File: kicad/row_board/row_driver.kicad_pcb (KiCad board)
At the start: 2 copper layers, 76 parts, among them J1 Panel row connector (female), J2 Row daisy chain connector (ma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, J5 EXT_CONTROL, J6 Barrel_Jack, Q1 2N3904, U1 TPIC6B595, U10 TXB0108-PWR, U2 TPIC6B595, U3 TBD62783, U4 TPIC6B595, U5 TPIC6B595, U6 TBD62783, U7 WE-FDSM_DC/DC_5V, U8 4N25, U9 WeMos_mini

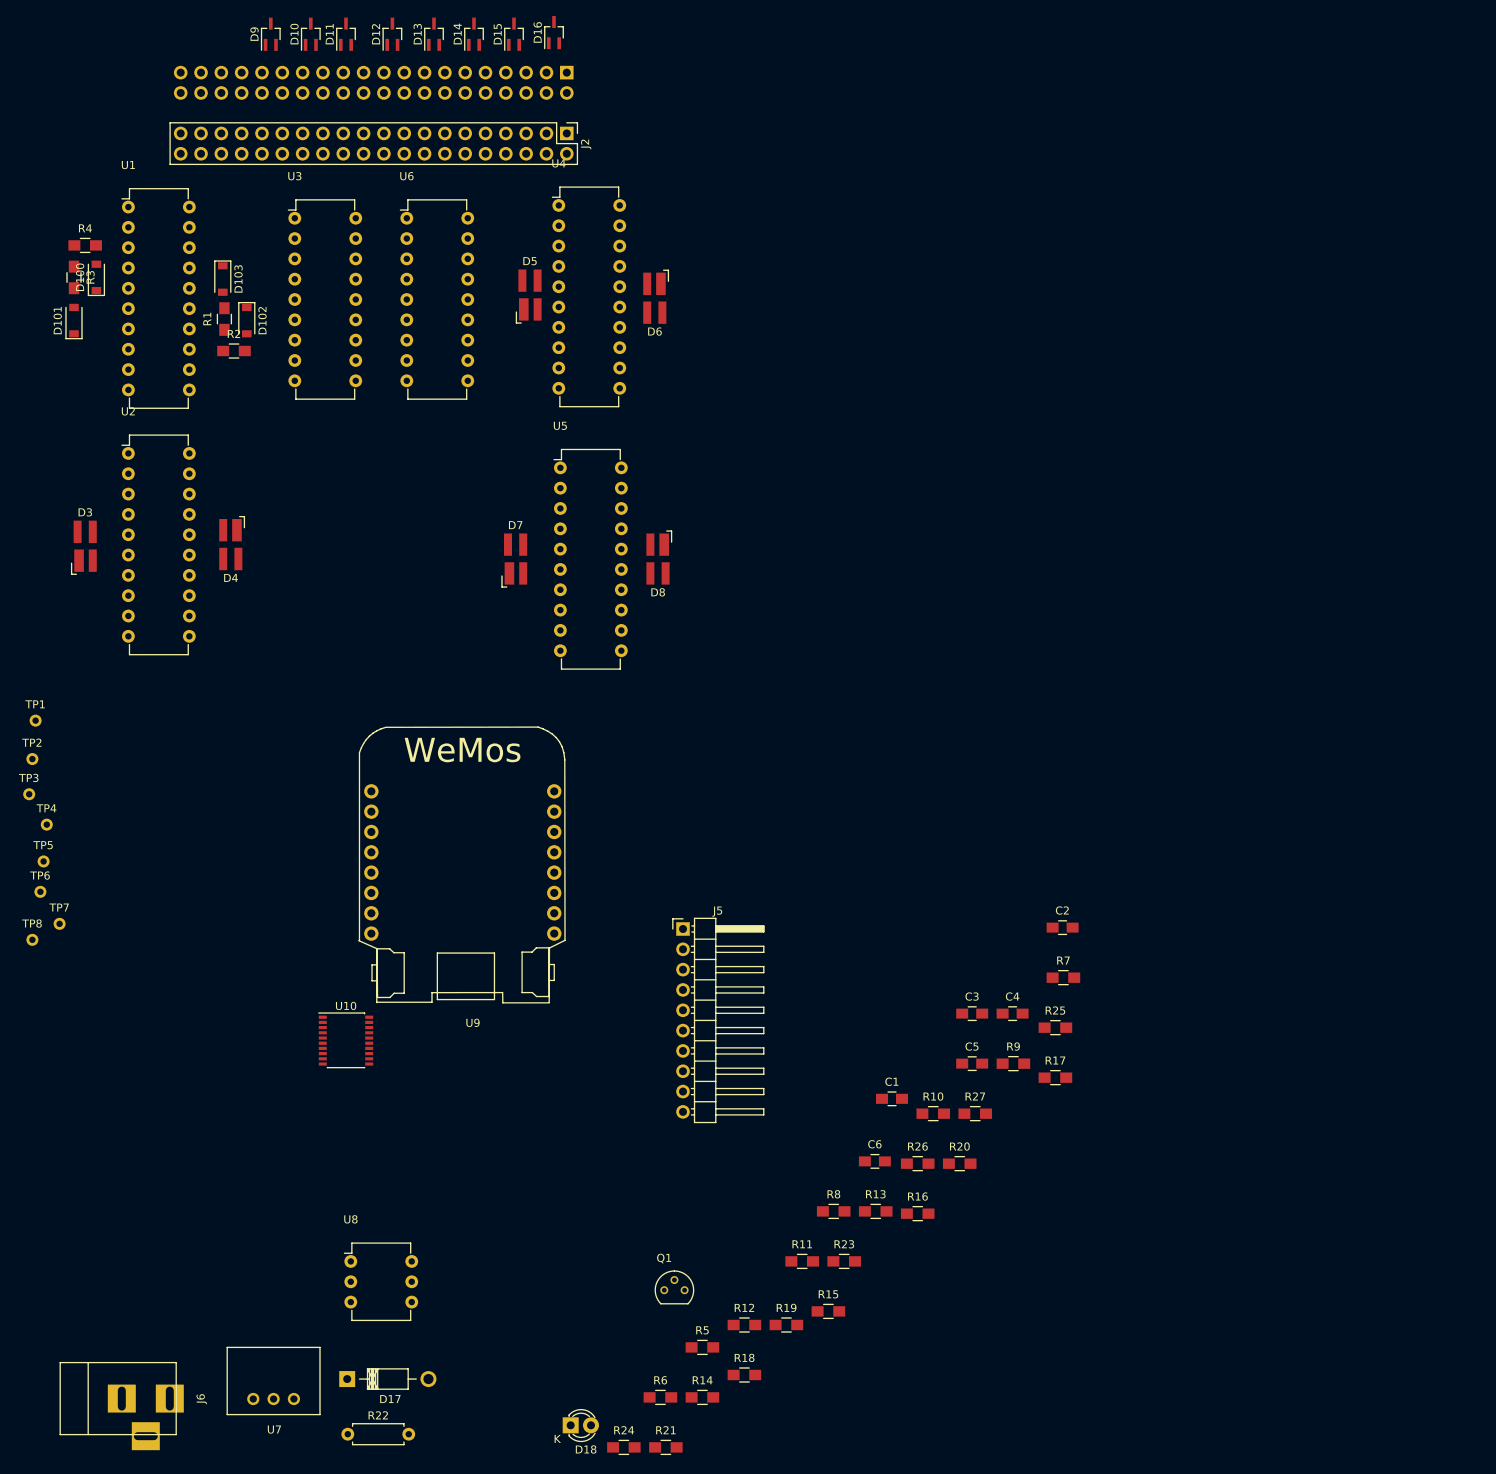
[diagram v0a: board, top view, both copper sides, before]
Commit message: Replace BAV23 with BAS16GW
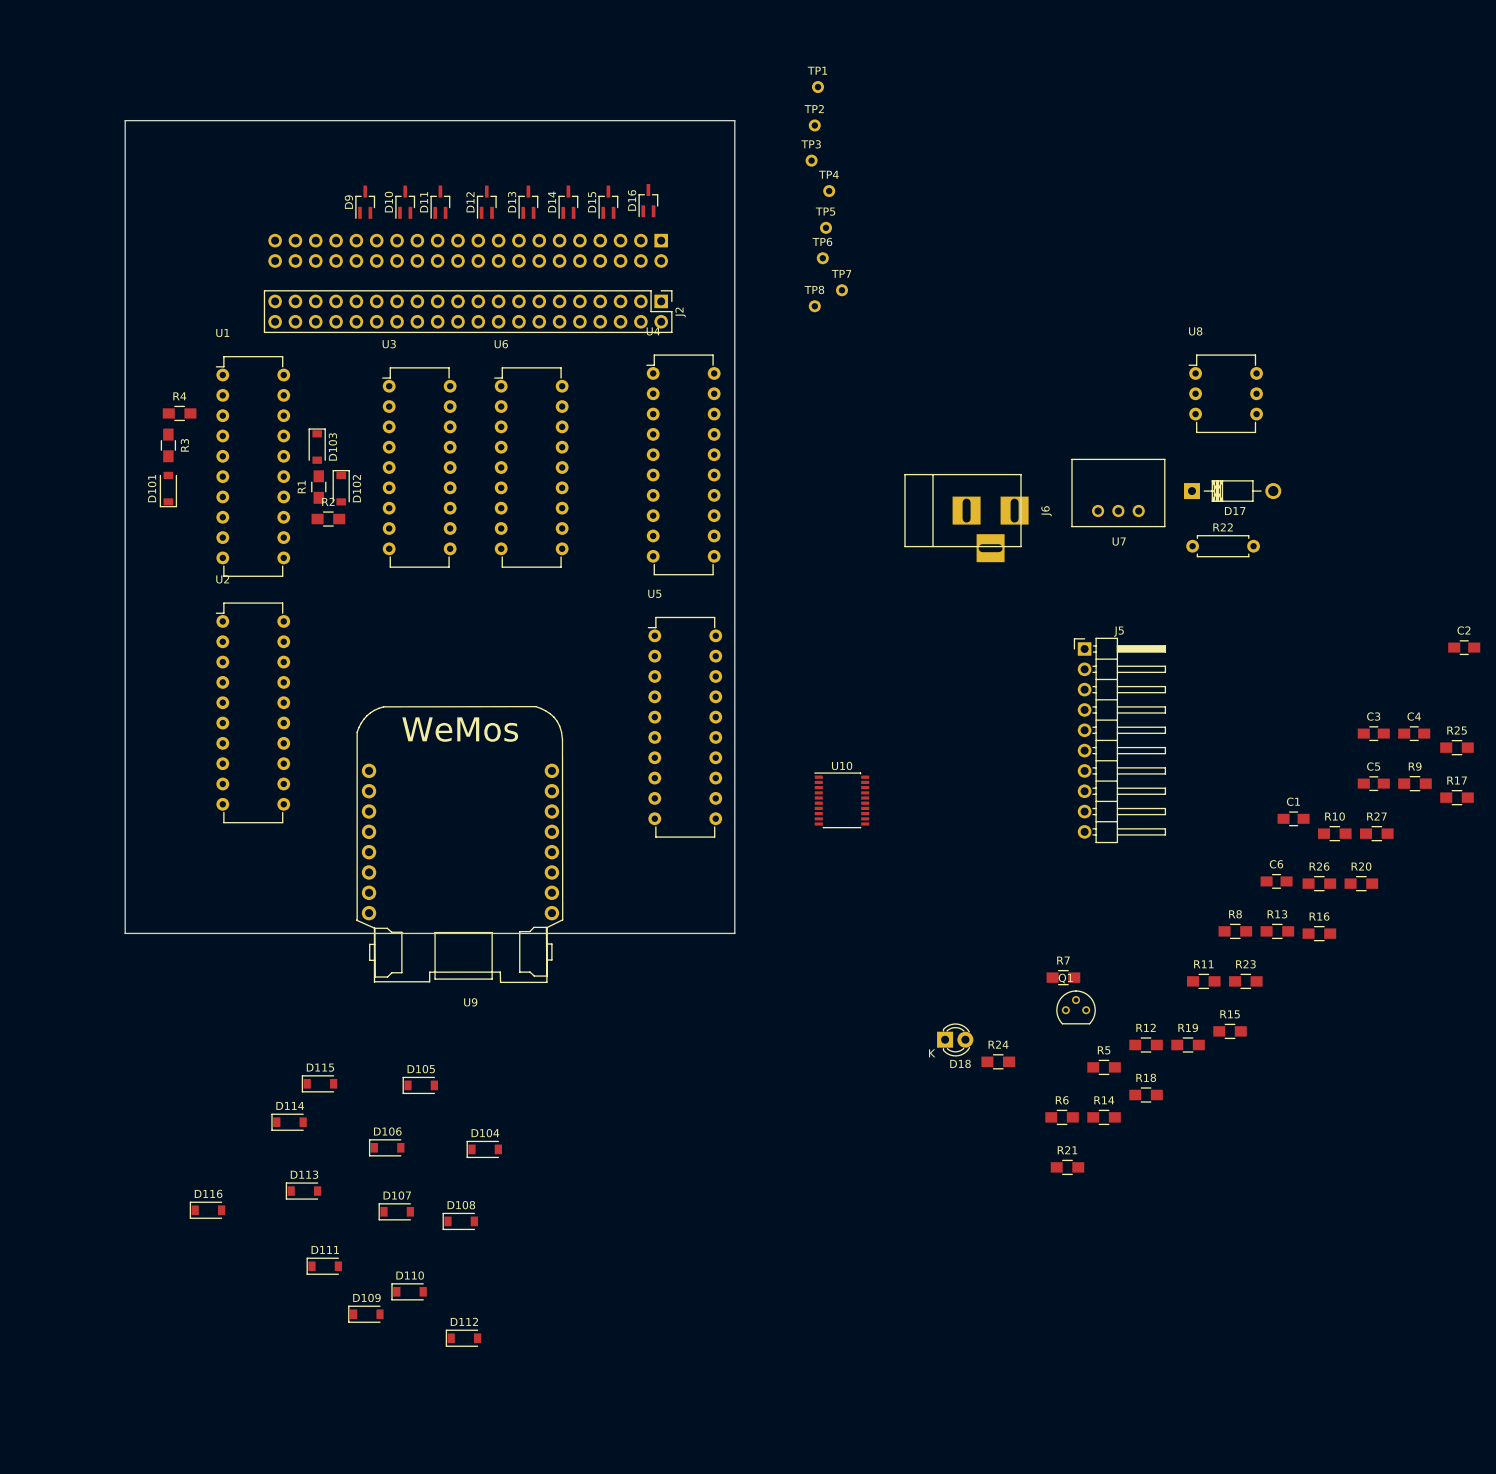
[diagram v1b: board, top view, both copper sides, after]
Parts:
- removed D100: D, Diodes_SMD:D_SOD-123
- removed D3, D4, D5, D6, D7, D8: BAV23, TO_SOT_Packages_SMD:SOT-143_Handsoldering
- added D104: BAS16GW, Diodes_SMD:D_SOD-123, F.Cu at (95.8, 154.0)
- added D105: BAS16GW, Diodes_SMD:D_SOD-123, F.Cu at (87.8, 146.0)
- added D106: BAS16GW, Diodes_SMD:D_SOD-123, F.Cu at (83.6, 153.8)
- added D107: BAS16GW, Diodes_SMD:D_SOD-123, F.Cu at (84.8, 161.8)
- added D108: BAS16GW, Diodes_SMD:D_SOD-123, F.Cu at (92.8, 163.0)
- added D109: BAS16GW, Diodes_SMD:D_SOD-123, F.Cu at (81.0, 174.6)
- added D110: BAS16GW, Diodes_SMD:D_SOD-123, F.Cu at (86.4, 171.8)
- added D111: BAS16GW, Diodes_SMD:D_SOD-123, F.Cu at (75.8, 168.6)
- added D112: BAS16GW, Diodes_SMD:D_SOD-123, F.Cu at (93.2, 177.6)
- added D113: BAS16GW, Diodes_SMD:D_SOD-123, F.Cu at (73.2, 159.2)
- added D114: BAS16GW, Diodes_SMD:D_SOD-123, F.Cu at (71.4, 150.6)
- added D115: BAS16GW, Diodes_SMD:D_SOD-123, F.Cu at (75.2, 145.8)
- added D116: BAS16GW, Diodes_SMD:D_SOD-123, F.Cu at (61.2, 161.6)
- D101, D102, D103: value D -> BAS16GW
- moved R22 153.2 mm to (184.2, 78.6)
- moved U8 153.2 mm to (184.6, 57.0)
- moved D17 153.2 mm to (184.1, 71.7)
- moved J6 153.2 mm to (155.8, 74.1)
- moved U7 153.2 mm to (174.9, 71.9)
- moved TP2 125.8 mm to (137.0, 26.0)
- moved TP1 125.8 mm to (137.4, 21.2)
- moved TP4 125.8 mm to (138.8, 34.2)
- moved TP5 125.8 mm to (138.4, 38.8)
- moved TP7 125.8 mm to (140.4, 46.6)
- moved TP3 125.8 mm to (136.6, 30.4)
- moved TP6 125.8 mm to (138.0, 42.6)
- moved TP8 125.8 mm to (137.0, 48.6)
- moved U10 68.9 mm to (140.4, 110.4)
- moved D18 67.2 mm to (153.3, 140.3)
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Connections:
- D101 pad 1: ROW15_L -> ROW16_L
- D102 pad 1: ROW14_L -> ROW15_L
- D103 pad 1: ROW13_L -> ROW14_L
- R1 pad 2: Net-(D103-Pad2) -> Net-(D104-Pad2)
- R2 pad 2: Net-(D102-Pad2) -> Net-(D103-Pad2)
- R3 pad 2: Net-(D101-Pad2) -> Net-(D102-Pad2)
- R4 pad 2: Net-(D100-Pad2) -> Net-(D101-Pad2)
- U1 pad 14: Net-(D102-Pad2) -> Net-(D103-Pad2)
- U1 pad 16: Net-(D103-Pad2) -> Net-(D104-Pad2)
- U1 pad 4: Net-(D100-Pad2) -> Net-(D101-Pad2)
- U1 pad 6: Net-(D101-Pad2) -> Net-(D102-Pad2)
- U3 pad 1: Net-(D100-Pad2) -> Net-(D101-Pad2)
- U3 pad 2: Net-(D101-Pad2) -> Net-(D102-Pad2)
- U3 pad 3: Net-(D102-Pad2) -> Net-(D103-Pad2)
- U3 pad 4: Net-(D103-Pad2) -> Net-(D104-Pad2)
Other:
- board outline added: 76.2 x 101.6 mm

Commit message: Begin layout
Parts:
- added J3: Conn_01x04, Connector_JST:JST_VH_B4PS-VH_1x04_P3.96mm_Horizontal, F.Cu at (109.8, 108.7)
- added J4: Conn_02x05_Odd_Even, Connectors:IDC_Header_Straight_10pins, F.Cu at (32.0, 107.7)
- added R28: 2K7, lib_fp:R_0805, F.Cu at (30.0, 70.1)
- C1, C2, C3, C4, C5, C6: footprint Capacitors_SMD:C_0805_HandSoldering -> lib_fp:C_0805
- D10, D11, D12, D13, D14, D15, D16, D9: footprint TO_SOT_Packages_SMD:SOT-323_SC-70_Handsoldering -> TO_SOT_Packages_SMD:SOT-323_SC-70
- D101, D102, D103, D104, D105, D106, D107, D108, D109, D110, D111, D112, D113, D114, D115, D116: footprint Diodes_SMD:D_SOD-123 -> lib_fp:D_SOD-123
- J2: footprint Pin_Headers:Pin_Header_Straight_2x20_Pitch2.54mm -> Connectors:IDC_Header_Straight_40pins
- J5: value EXT_CONTROL -> Conn_01x10
- R1, R10, R11, R12, R13, R14, R15, R16, R17, R18, R19, R2, R20, R21, R23, R24, R25, R26, R27, R3, R4, R5, R6, R7, R8, R9: footprint Resistors_SMD:R_0805_HandSoldering -> lib_fp:R_0805
- moved R17 199.0 mm to (33.5, 33.5)
- moved R25 190.9 mm to (35.1, 46.7)
- moved D17 186.4 mm to (-0.39, 45.6)
- moved R22 186.4 mm to (-0.31, 52.5)
- moved U8 186.4 mm to (0.07, 30.9)
- moved C5 185.5 mm to (34.5, 39.6), turned to 90 degrees
- moved C6 183.5 mm to (31.5, 36.6)
- moved Q1 182.5 mm to (14.0, 39.4)
- moved R23 177.3 mm to (29.8, 58.8)
- moved D18 176.6 mm to (14.0, 31.8)
- moved R20 175.6 mm to (49.4, 40.0)
- moved R27 175.6 mm to (51.3, 33.8)
- moved R26 170.0 mm to (48.3, 44.2)
- moved C1 160.1 mm to (43.7, 66.0)
- moved R21 158.3 mm to (53.3, 47.8)
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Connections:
- net /COL_EN renamed ~COL_EN
- net /COL_EN_3v3 renamed ~COL_EN_3v3
- net /RC_CLR renamed ~RC_CLR
- net /RC_CLR_3v3 renamed ~RC_CLR_3v3
- net /ROW_EN renamed ~ROW_EN
- net /ROW_EN_3v3 renamed ~ROW_EN_3v3
- net /SENSE renamed ~SENSE
- net ROW_DATA_OUT renamed RC_DATA_OUT
- R1 pad 2: Net-(D104-Pad2) -> Net-(D101-Pad2)
- R10 pad 2: Net-(D111-Pad2) -> Net-(D110-Pad2)
- R11 pad 2: Net-(D110-Pad2) -> Net-(D111-Pad2)
- R12 pad 2: Net-(D109-Pad2) -> Net-(D112-Pad2)
- R2 pad 2: Net-(D103-Pad2) -> Net-(D102-Pad2)
- R3 pad 2: Net-(D102-Pad2) -> Net-(D103-Pad2)
- R4 pad 2: Net-(D101-Pad2) -> Net-(D104-Pad2)
- R9 pad 2: Net-(D112-Pad2) -> Net-(D109-Pad2)
- U10 pad 12: SENSE_EN -> Net-(U10-Pad12)
- U10 pad 9: SENSE_EN_3v3 -> Net-(U10-Pad9)
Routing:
- net ROW2_L: track 0.00 -> 9.94 mm
- net ROW1_H: track 0.00 -> 9.94 mm
- net ROW1_L: track 0.00 -> 9.94 mm
- net ROW2_H: track 0.00 -> 9.90 mm
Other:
- board size 76.2 x 101.6 mm -> 100 x 100 mm
- net class Default: via_dia 0.6 -> 1; via_drill 0.4 -> 0.5
- net class High Current added: clearance 0.2, trace_width 0.35, via_dia 1.2, via_drill 0.7
- rule trace_min: 0.2 -> 0.127
- rule via_min_size: 0.4 -> 0.6

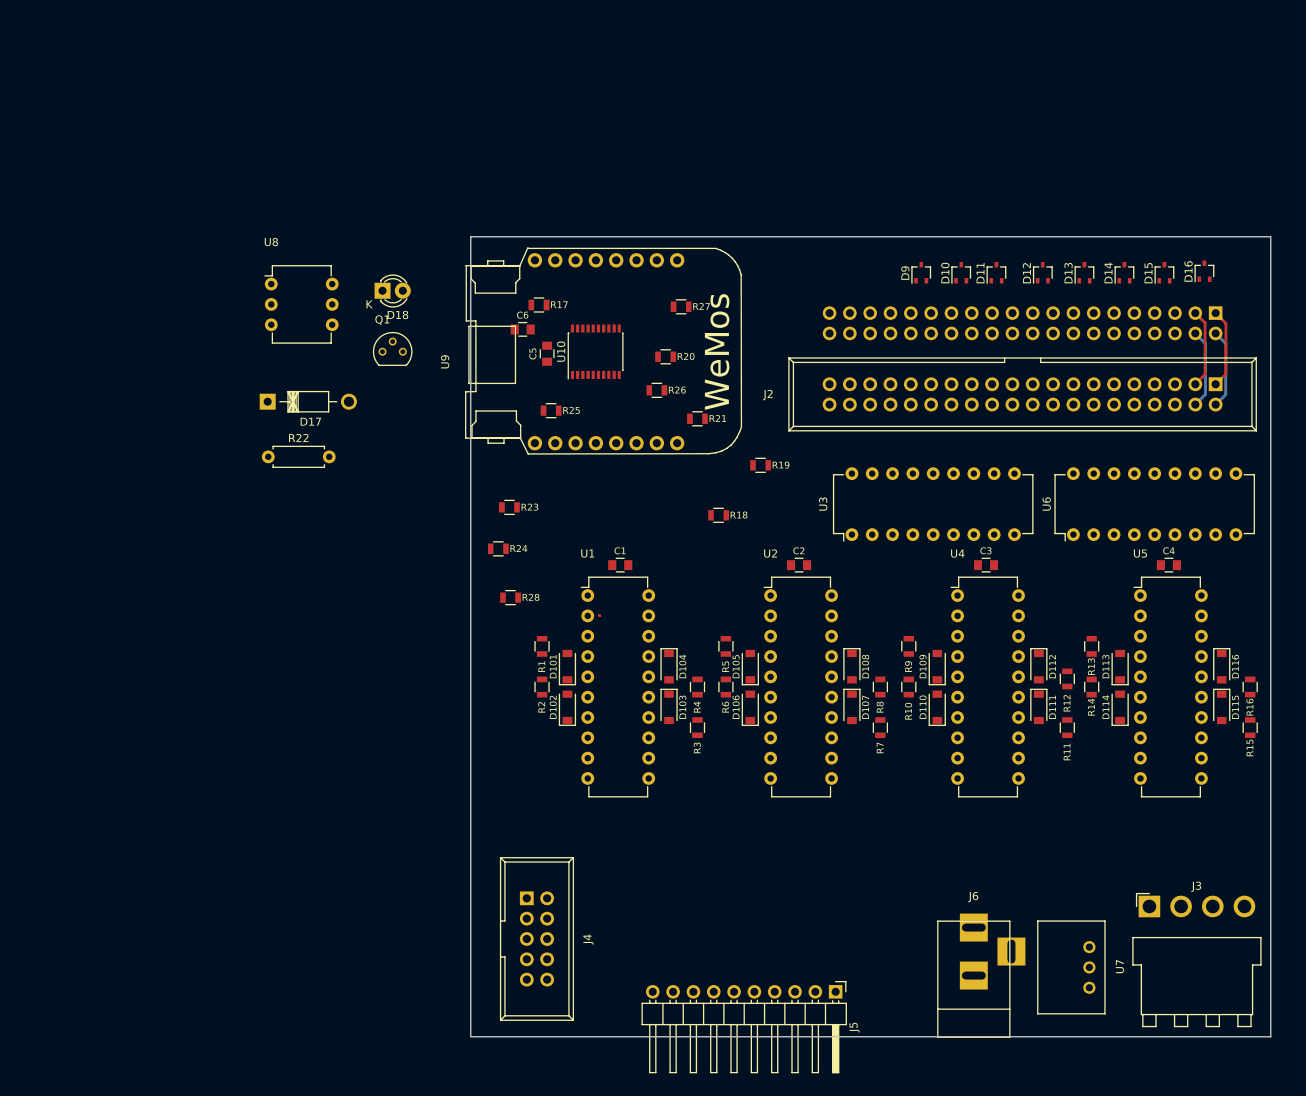
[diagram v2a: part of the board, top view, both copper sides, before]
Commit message: Add reverse power protection; data sheets
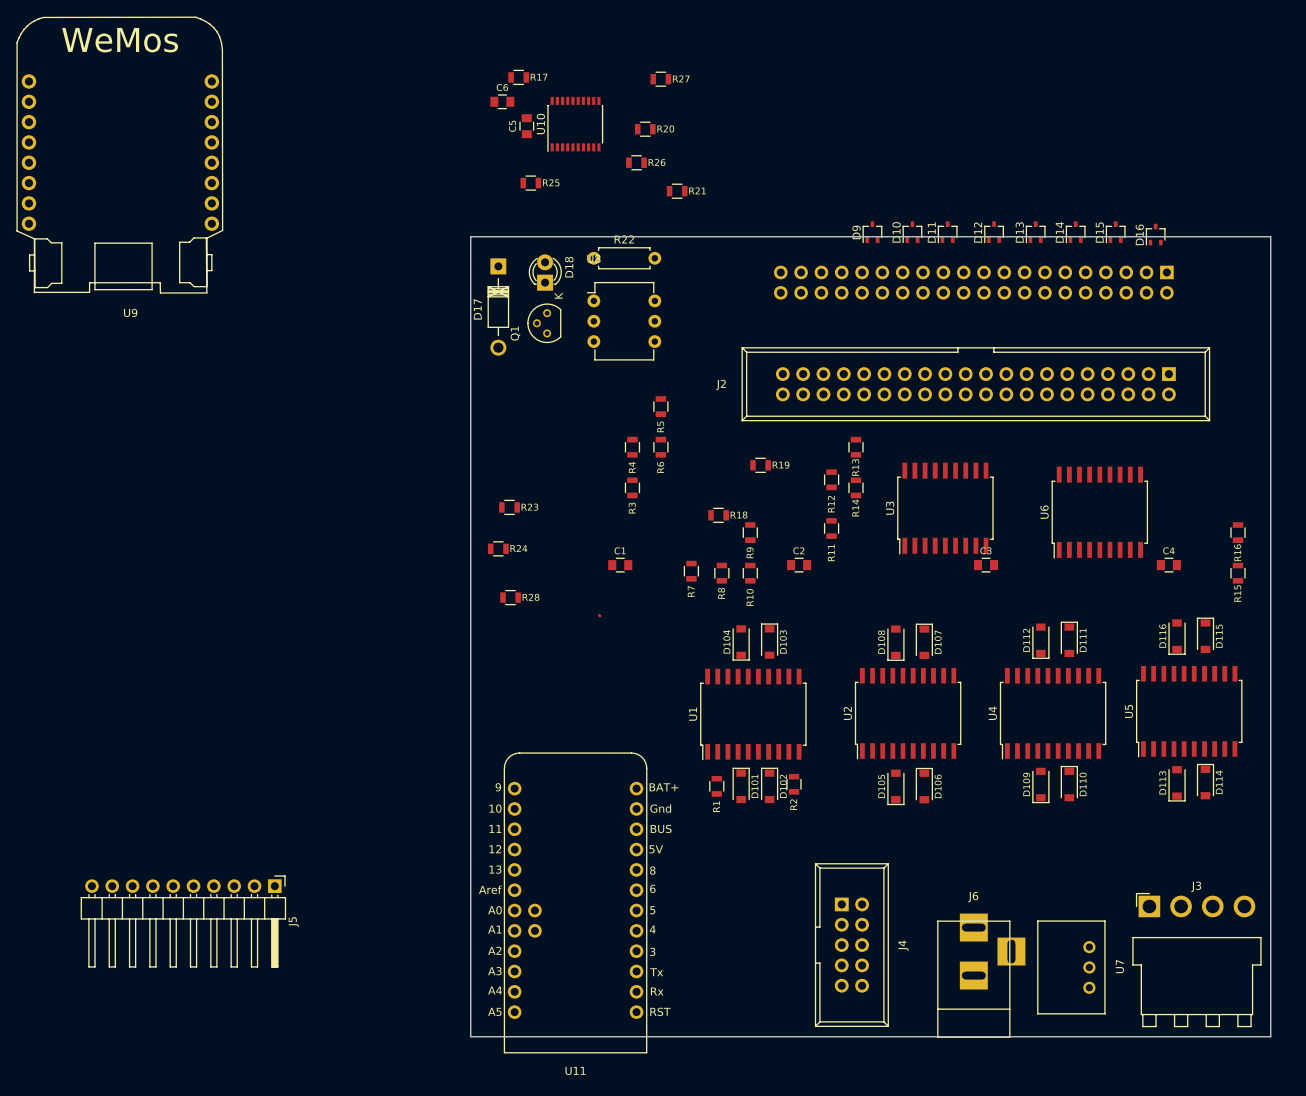
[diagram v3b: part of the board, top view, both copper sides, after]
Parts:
- added U11: AdafruitProTrinket5V, lib_fp:Adafruit_Trinket_Pro, F.Cu at (38.1, 108.0)
- R24: value 1K2 -> 2K2
- U1, U2, U4, U5: footprint Housings_DIP:DIP-20_W7.62mm -> Housings_SOIC:SOIC-20W_7.5x12.8mm_Pitch1.27mm
- U3, U6: footprint Housings_DIP:DIP-18_W7.62mm -> Housings_SOIC:SOIC-18W_7.5x11.6mm_Pitch1.27mm
- moved J5 71.3 mm to (0.51, 106.2)
- moved U9 64.0 mm to (-18.8, 15.7), turned to 0 degrees
- moved R22 47.7 mm to (40.4, 27.7)
- moved U8 40.4 mm to (40.4, 33.0)
- moved J4 39.4 mm to (71.4, 108.5)
- moved R13 38.6 mm to (73.2, 51.3)
- moved R14 38.6 mm to (73.2, 56.4)
- moved R11 38.6 mm to (70.1, 61.5)
- moved R12 38.6 mm to (70.1, 55.4)
- moved R2 33.8 mm to (65.4, 93.4)
- moved D17 33.4 mm to (28.4, 28.7), turned to 270 degrees
- moved R3 31.1 mm to (45.2, 56.4)
- moved R4 31.1 mm to (45.2, 51.3)
- moved R5 31.1 mm to (48.8, 46.2)
- moved R6 31.1 mm to (48.8, 51.3)
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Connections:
- J4 pad 10: Net-(J4-Pad10) -> GND
- J4 pad 2: Net-(J4-Pad2) -> GND
- J4 pad 4: Net-(J4-Pad4) -> GND
- J4 pad 6: Net-(J4-Pad6) -> GND
- J4 pad 8: Net-(J4-Pad8) -> GND
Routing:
- net ROW2_L: track 9.94 -> 0.00 mm
- net ROW1_H: track 9.94 -> 0.00 mm
- net ROW1_L: track 9.94 -> 0.00 mm
- net ROW2_H: track 9.90 -> 0.00 mm
